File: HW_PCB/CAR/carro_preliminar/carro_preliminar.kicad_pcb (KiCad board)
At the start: 2 copper layers, 57.4 x 41.3 mm, 45 parts, among them IC1 TB6612FNG, J1 V_Battery, J2 STLINK, J3 Motores, J4 BATTLEDS, J5 UART, J6 Servo_Motor, J7 NRF24L01, J8 Conn_01x03_Pin, SW1 SW_DPST_x2, U1 STM32F103C8Tx, U2 AMS1117-3.3, U3 AMS1117-3.3, U5 AMS1117-5.0, Y1 8MHz

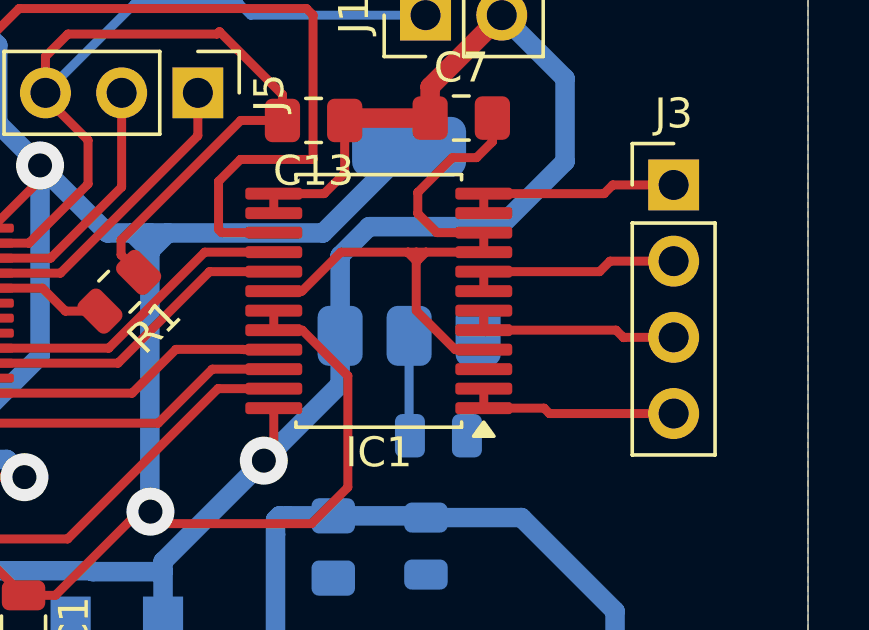
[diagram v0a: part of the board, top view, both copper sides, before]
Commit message: Corregido uncexion en gnd del driver
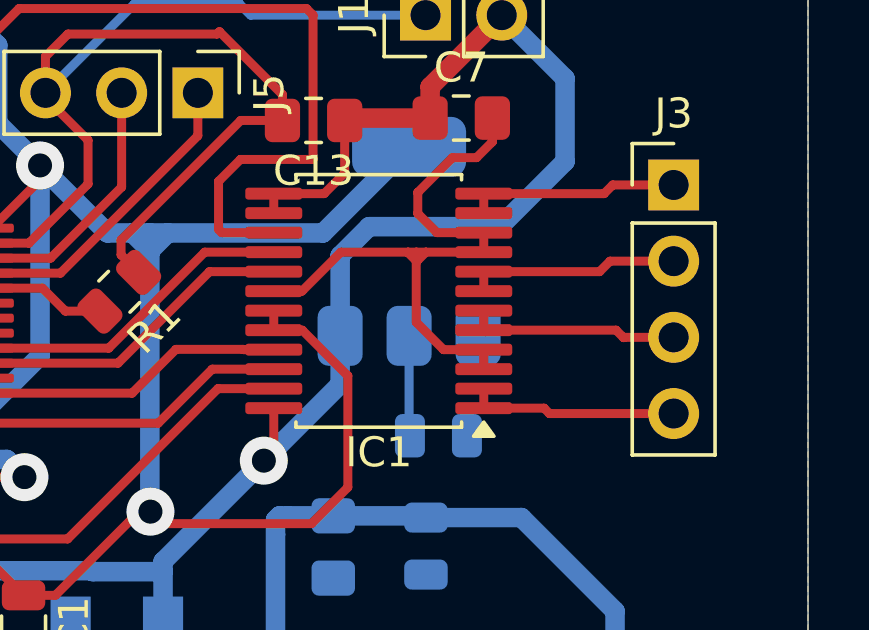
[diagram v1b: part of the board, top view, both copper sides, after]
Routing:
- net GND: track 131.0 -> 131.9 mm
